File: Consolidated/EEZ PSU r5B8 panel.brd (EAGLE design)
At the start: 316 x 150 mm, 799 parts, among them IC1 LTC3864, IC10 REF5025, IC11 DAC8552, IC12 ADG465SOT-23, IC13 TS5A9411DCKT, IC14 ADS1120, IC15 LP339D, IC16 LM25575, IC17 MC7812, IC18 TPD4E002DRLR, IC19 TPD2E001DZDR, IC2 MC79L05, IC20 ADUM3160BRWZ, IC21 TLC5925IDBQR, IC22 Si8641EC-B-IS1, IC23 SI8651EC-B-IS1, IC24 SI8651EC-B-IS1, IC25 LD1117ADT33TR, IC26 Si8641EC-B-IS1, IC27 PCA21125, IC28 AT25256B, IC29 W5500, IC3 MC78L05, IC30 BC857BS, IC31 TLC555, IC32 SN74LVC2G08DCTR, IC33 TPS3705-33D, IC34 SN74LV1T34DBVR, IC35 SN74LVC2G02DCTR, IC36 DAC8552, IC37 ADS1120, IC38 MCP23S08-E/SO, IC39 OP27GSZ, IC4 LM5574, IC40 TL072D, IC41 TL072D, IC42 REF5025, IC43 LTC3864, IC44 LM5574, IC45 MC79L05, IC46 MC78L05, IC47 TS5A9411DCKT, IC48 ADG465SOT-23, IC49 LP339D, IC5 LP2951SO8, IC50 LP2951SO8, IC6 TL072D, IC7 TL072D, IC8 OP27GSZ, IC9 MCP23S08-E/SO, J1 BS-244DSM-R, J2 BS-244DSM-G, J3 BS-244DSM-B, J4 BS-244DSM-R, J5 BS-244DSM-B, Q1 SUD19P06-60, Q10 MMBT5401, Q11 MMBT5401, Q12 MMBT5551, Q13 MMBT5551, Q14 BSS84P, Q15 2N7002, Q16 MMBT5551, Q17 MMBT5401, Q18 MMBT5551, Q19 MMBT5551, Q2 MMBT5401, Q20 BTA26-600, Q21 BTA26-600, Q22 IRLL014N, Q23 IRLML2246TRPBF, Q24 IRLML2246TRPBF, Q25 IRLML2246TRPBF, Q26 IRLML2246TRPBF, Q27 2N7002, Q28 IRLML2246TRPBF, Q29 2N7002, Q3 2N7002, Q30 2N7002, Q31 IRFP250N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

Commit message: Consolidated PCB, jumpers renumbering
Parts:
- removed JMP1, JMP2: 0R-JUMPA, jump-0r-smd:A0R-JMP
- added JP6, JP7: 0R-JUMPA, jump-0r-smd:A0R-JMP
- C18, C239: value EEEFK1J470P -> EEEFK1J101P
- D28: device diode:DO214AC -> EEZ_Lib1:SOD123
- FB6, FB7: value 2506033007Y3 -> 60R@100MHz
- JP1: value 826926-2 -> 0R-JUMPA; device jumper:JP1 -> jump-0r-smd:A0R-JMP
- JP3: value 0R-JUMPA -> 826926-2; device jump-0r-smd:A0R-JMP -> jumper:JP1
- L16, L2: value See Note 1.2 -> 7443551331
- LED1, LED2: device led:CHIPLED_0805 -> EEZ_Lib1:LED_0805
- R12, R217: value See Note 1.3 -> 324K
- moved JP2 301.9 mm to (15.5, 134.0), turned to 90 degrees
- moved JP1 128.8 mm to (107.6, 125.8), turned to 180 degrees
- moved JP3 80.8 mm to (224.2, 71.1), turned to 90 degrees
- moved JP4 24.5 mm to (307.8, 58.8)
- moved JP5 12.2 mm to (299.5, 42.0)
- renumbered JMP3 to JP8, JMP4 to JP9
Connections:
- net !INT: now also JP2.2; no longer JMP2.2
- net !PS_DRDY: now also JP2.3; no longer JMP2.3
- net !PWD_RST: now also JP3.1; no longer JP1.1
- net +3V3: now also JP4.3; no longer JP2.3
- net +5V: now also JP4.1; no longer JP2.1
- net GND: now also JP3.2; no longer JP1.2
- net INT_EXP: now also JP2.1; no longer JMP2.1
- net MISO: now also JP7.1; no longer JP5.1
- net MODE: now also JP1.2; no longer JMP1.2
- net MOSI: now also JP6.1; no longer JP4.1
- net N$102: now also JP4.2; no longer JP2.2
- net N$104: now also JP7.2; no longer JP5.2
- net N$105: now also JP5.2; no longer JP3.2
- net N$106: now also JP6.2; no longer JP4.2
- net SCLK: now also JP5.1; no longer JP3.1
- net SGND: now also JP1.1; no longer JMP1.1
- net SYNC: now also JP1.3; no longer JMP1.3
- net TOUCH_DIN: now also JP6.3; no longer JP4.3
- net TOUCH_DOUT: now also JP7.3; no longer JP5.3
- net TOUCH_SCLK: now also JP5.3; no longer JP3.3
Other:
- board text added: "JP6"
- board text added: "JP7"
- board text removed: "Alu thermal bridge (5mm thick)"
- board text removed: "Copy here Power module for final panel!"
- board text removed: "JMP1"
- board text removed: "JMP2"

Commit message: Fixed fan control, miniMELF replaced with SOD-323
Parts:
- added C240: EEEFK1J101P, EEZ_Lib1:PANASONIC_F
- added D47: SKL16, EEZ_Lib1:SOD123
- C104: value 470n/100V -> 100n; device rcl:C1812 -> rcl:C0603
- C105, C110: value 10n -> 470n/100V; device rcl:C1206 -> rcl:C1812
- C106, C111: value UPW1J150MED -> 10n; device MyLib6:CAPAE660X610N_COMBO2 -> rcl:C1206
- C107: value 10u -> UPW1J150MED; device rcl:C1206 -> MyLib6:CAPAE660X610N_COMBO2
- C108: value 10n -> 10u
- C109: value 470n/100V -> 10n; device rcl:C1812 -> rcl:C1206
- C112: value 10n -> UPW1J150MED; device rcl:C1206 -> MyLib6:CAPAE660X610N_COMBO2
- C113: value 100n -> 10n; device rcl:C0603 -> rcl:C1206
- C119: value 47u -> 100n; device MyLib6:PANASONIC_C -> rcl:C0603
- C120: value 10u -> 47u
- C121: value 100n -> 10u; device rcl:C0603 -> MyLib6:PANASONIC_C
- C125: value 10u -> 100n; device rcl:C1206 -> rcl:C0603
- C126, C162: value 100n -> 10u; device rcl:C0603 -> rcl:C1206
- C127: value EECS5R5H105 -> 100n; device EEZ_Lib1:SG-R20MM -> rcl:C0603
- C128: value 100n -> EECS5R5H105; device rcl:C0603 -> EEZ_Lib1:SG-R20MM
- C130: value 22n -> 100n; device rcl:C0805 -> rcl:C0603
- C131: value 18p -> 22n
- C132: value 6n8 -> 18p; device rcl:C0603 -> rcl:C0805
- C133: value 10n -> 6n8; device rcl:C0805 -> rcl:C0603
- C134: value 6n8 -> 10n; device rcl:C0603 -> rcl:C0805
- C135: value 18p -> 6n8; device rcl:C0805 -> rcl:C0603
- C136: value 100n -> 18p; device rcl:C0603 -> rcl:C0805
- C144: value 10u -> 100n; device EEZ_Lib1:EC1206 -> rcl:C0603
- C145, C193, C223: value 4u7 -> 10u
- C146: value 10n -> 4u7; device rcl:C0805 -> EEZ_Lib1:EC1206
- C147, C156, C178, C183: value 100n -> 10n; device rcl:C0603 -> rcl:C0805
- C148, C152: value 47n -> 100n; device rcl:C0805 -> rcl:C0603
- C149, C153, C99: value 100n -> 47n; device rcl:C0603 -> rcl:C0805
- C154: value 10n -> 100n; device rcl:C0805 -> rcl:C0603
- C158, C174: value 1n -> 100n; device rcl:C0805 -> rcl:C0603
- C159: value 100n -> 1n; device rcl:C0603 -> rcl:C0805
- C160: value 120p -> 100n; device rcl:C0805 -> rcl:C0603
- C161: value 10u -> 120p; device rcl:C1206 -> rcl:C0805
- C168: value 47p -> 100n; device rcl:C0805 -> rcl:C0603
- C169, C171: value 2n2 -> 47p
- C170: value 47p -> 2n2
- C172: value 100n -> 2n2; device rcl:C0603 -> rcl:C0805
- C177: value 10n -> 1n
- C179, C185: value 1u -> 100n; device rcl:C0805 -> rcl:C0603
- C180, C182: value 10n -> 1u
- C181: value 1u -> 10n
- C188: value 470n -> 1u; device rcl:C1812 -> rcl:C0805
- C189: value 4u7 -> 470n; device rcl:C1210 -> rcl:C1812
- C190: value 10u -> 4u7
- C191: value 330p -> 10u; device rcl:C0805 -> rcl:C1210
- C192: value 10u -> 330p; device rcl:C1210 -> rcl:C0805
- C194: value 4n7 -> 4u7; device rcl:C0805 -> rcl:C1210
- C195: value 120p -> 4n7
- C196: value 1u -> 120p; device rcl:C1206 -> rcl:C0805
- C197: value 470n -> 1u; device rcl:C0805 -> rcl:C1206
- C198: value 100n -> 470n
- C201: value 1u -> 100n; device resistor:C1206 -> rcl:C0805
- C203: value 2u2 -> 1u; device rcl:C0805 -> resistor:C1206
- C204: value 47u -> 2u2; device EEZ_Lib1:CAPAE660X610N -> rcl:C0805
- C206: value 2u2 -> 47u; device rcl:C0805 -> EEZ_Lib1:CAPAE660X610N
- C207: value 330n -> 2u2
- C208: value 3n3 -> 330n
- C209: value 1n -> 3n3
- C210: value 22n -> 1n
- C211: value 100n -> 22n
- C212: value 10n -> 100n
- C213: value 2u2/100V -> 10n; device rcl:C1210 -> rcl:C0805
- C214: value 2u2 -> 2u2/100V; device rcl:C0805 -> rcl:C1210
- C216: value 330p -> 2u2
- C217: value 2m2 -> 330p; device EEZ_Lib1:ECAP7.5/18 -> rcl:C0805
- C218: value 330n -> 2m2; device rcl:C0805 -> EEZ_Lib1:ECAP7.5/18
- C219: value 100n -> 330n
- C222: value 10u -> 100n; device EEZ_Lib1:EC1206 -> rcl:C0805
- C224: value 2m2 -> 4u7; device EEZ_Lib1:ECAP7.5/18 -> EEZ_Lib1:EC1206
- C225: value EEEFK1J470P -> 2m2; device Panasonic-EEEFK_EEEFP:CAPAE830X1050N -> EEZ_Lib1:ECAP7.5/18
- C226: value 470p -> EEEFK1J470P; device rcl:C0805 -> Panasonic-EEEFK_EEEFP:CAPAE830X1050N
- C227: value 4u7 -> 470p; device rcl:C1210 -> rcl:C0805
- C228: value 10n -> 4u7; device rcl:C0805 -> rcl:C1210
- C230: value 2n2 -> 10n
- C231: value 100n -> 2n2; device rcl:C1206 -> rcl:C0805
- C234: device rcl:C0603 -> rcl:C1206
- C235: value 3n3 -> 100n; device rcl:C0805 -> rcl:C0603
- C239: value EEEFK1J101P -> 3n3; device EEZ_Lib1:PANASONIC_F -> rcl:C0805
- C97: value 100u -> 10u; device EEZ_Lib1:CAPAE660X610N -> MyLib6:PANASONIC_C
- C98: value 47n -> 100u; device rcl:C0805 -> EEZ_Lib1:CAPAE660X610N
- D25: value SMBJ5.0A-TR -> BAS316; device MyLib6:DO214AA -> diode:SOD323-W
- D26: value BAS316 -> SMBJ5.0A-TR; device diode:SOD323-W -> MyLib6:DO214AA
- D27: value BAT54S -> BAS316; device diode:SOT23 -> diode:SOD323-W
- D28: value SKL16 -> BAT54S; device EEZ_Lib1:SOD123 -> diode:SOT23
- D29: value BAS316 -> SKL16; device diode:SOD323-W -> EEZ_Lib1:SOD123
- D37: value STPS15H100 -> BAS316; device EEZ_Lib1:TO252 -> diode:SOD323-W
- D38: value BAS316 -> STPS15H100; device diode:SOD323-W -> EEZ_Lib1:TO252
- D39: value DFLS1100-7 -> BAS316; device EEZ_Lib1:SOD123 -> diode:SOD323-W
- D41: value STPS15H100 -> DFLS1100-7; device EEZ_Lib1:TO252@1 -> EEZ_Lib1:SOD123
- D45: value SKL16 -> STPS15H100; device EEZ_Lib1:SOD123 -> EEZ_Lib1:TO252@1
- ZD13, ZD4: value 13V -> BZX384-C15.115; device EEZ_Lib1:MINIMELF -> EEZ_Lib1:SOD323-W
- ZD14, ZD5: value 6V2 -> PDZ6.2B; device EEZ_Lib1:MINIMELF -> EEZ_Lib1:SOD323-W
- moved D25 192.5 mm to (119.5, 52.1), turned to 0 degrees
- moved C119 165.9 mm to (135.4, 61.0), turned to 90 degrees
- moved EEZ_SIGNATURE 128.8 mm to (3.81, 79.8)
- moved EEZ_SIGNATURE3 128.8 mm to (155.8, 79.8)
- moved C104 125.8 mm to (68.7, 64.7)
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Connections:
- removed net GND7: C157.1, C159.1, C161.2, C162.1, C163.1, C164.2, C165.1, C166.1, C167.1, C172.1, C173.2, C177.2, C178.2, C179.1, C180.1, C181.1, C182.1, C183.1, C184.1, C185.1, C186.1, C187.2, C188.2, C189.2, C190.2, C192.2, C193.2, C196.2, C203.2, C204.1, C205.2, C206.2, C207.1, C208.1, C211.1, C212.2, C213.2, C214.2, C215.2, C217.-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
- removed net N$169 (its old number): C160.1, D30.C, IC40.2, R165.2, R178.2
- removed net N$176 (its old number): C171.1, R202.2, R204.1
- removed net N$198 (its old number): D36.A, Q39.C, Q42.1, R186.2
- removed net N$211 (its old number): C158.1, R175.1
- removed net N$214 (its old number): C187.1, IC42.5
- removed net N$220 (its old number): C160.2, R216.1
- removed net N$229 (its old number): C198.2, IC43.4
- removed net N$234 (its old number): C209.2, R230.2
- removed net N$239 (its old number): C211.2, IC44.1
- removed net N$243 (its old number): C216.2, R235.2
- removed net N$251 (its old number): C228.2, Q47.B, R244.1, R245.2, R246.2
- removed net N$254 (its old number): C229.1, Q46.B, R247.2, R248.1
- removed net N$257 (its old number): C223.+, FB12.P$1, IC50.1, R237.1, R239.1
- removed net N$259 (its old number): C235.2, IC37.10, R255.2
- new net GND1: C158.1, C160.1, C162.2, C163.1, C164.1, C165.2, C166.1, C167.1, C168.1, C173.1, C174.2, C178.2, C179.2, C180.1, C181.1, C182.1, C183.1, C184.1, C185.1, C186.1, C187.1, C188.2, C189.2, C190.2, C191.2, C193.2, C194.2, C197.2, C204.2, C205.1, C206.2, C207.2, C208.1, C209.1, C212.1, C213.2, C214.2, C215.2, C216.2, C218.-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
- new net N$163: D21.C, X6.3
- new net N$173: C166.2, C186.2, IC37.12, R166.2
- new net N$197: D36.C, ZD14.C
- new net N$199: D37.A, Q39.C, Q42.1, R186.2
- new net N$212: C159.1, R175.1
- new net N$215: C188.1, IC42.5
- new net N$227: C198.1, IC43.9
- new net N$233: C204.1, D41.A, L13.1
- new net N$237: C211.2, IC44.16
- new net N$242: C213.1, IC44.10
- new net N$246: C221.1, D47.C, FB11.P$1, IC46.1
- new net N$253: C231.2, Q47.C, R249.1, R251.2
- new net N$256: C231.1, Q48.B, R249.2, R250.2
- new net N$258: C224.+, FB12.P$1, IC50.1, R237.1, R239.1
- new net N$263: C239.1, IC37.6, R258.2
- net !MR: now also C153.2; no longer C152.2
- net +3V3: now also C108.1, C116.1, C118.1, C121.1, C123.1, C127.1, C131.1, C137.2, C144.1, C145.+, C150.2, C151.1, C152.2, C154.1, C157.1, D27.A; no longer C107.1, C114.1, C117.1, C120.1, C122.1, C126.1, C130.1, C136.2, C138.1, C144.+, C149.2, C150.1, C151.2, C153.1, C156.1, D26.A
- net +5V: now also C100.1, C120.1, C126.2, D26.C; no longer C119.1, C125.2, C99.1, D25.C
- net +5V1: now also C163.2, C165.1, C167.2, C187.2; no longer C162.2, C164.1, C166.2, C186.2
- net +VNR1: now also C207.1, C220.1; no longer C206.1, C218.1
- net +VREF1: now also C164.2, C223.+, C235.2; no longer C163.2, C222.+, C234.2
- net -9V1: now also C205.2, C208.2; no longer C204.2, C207.2
- net 12VDC: now also C98.1
- net 1V2O: now also C147.2; no longer C146.2
- net AC_IN1: now also X2.1; no longer X2.2
- net AC_IN2: now also X2.2; no longer X2.1
- net AC_IN3: now also D42.1, D42.2, D44.3, X22.2; no longer D41.1, D41.2, D43.3, X22.1
- net AC_IN4: now also D43.1, D43.2, D45.3, X22.1; no longer D42.1, D42.2, D44.3, X22.2
- net AUX_FAN_SENSE: now also D21.A; no longer X6.3
- net CH1_GND: now also C114.2, C117.2, C148.2, C149.1; no longer C113.2, C116.2, C147.2, C148.1
- net CH1_VDD: now also C114.1, C117.1, C148.1; no longer C113.1, C116.1, C147.1
- net CH2_GND: now also C119.2, C122.2; no longer C118.2, C121.2
- net CH2_VDD: now also C119.1, C122.1; no longer C118.1, C121.1
- net DC+: now also L1.2; no longer L1.1
- net DC+1: now also C234.2, L17.2; no longer C233.2, L17.1
- net DC-: now also L1.1, X1.3; no longer L1.2, X1.1
- net DC-1: now also C234.1, L17.1, X23.3; no longer C233.1, L17.2, X23.1
- net DC_OUT: now also L1.3; no longer L1.4
- net DC_OUT1: now also C190.1, C194.1, C197.1, C198.2, C218.+, C225.+, C228.1, C232.2, D43.3, L17.3; no longer C188.1, C193.1, C196.1, C197.2, C217.+, C224.+, C227.1, C231.2, D41.3, L17.4
- net DC_PREG3: now also C214.1; no longer C213.1
- net EARTH: now also C106.2, C109.1, C111.2, C113.1, C131.2, C134.2, X1.1; no longer C105.2, C108.1, C110.2, C112.1, C130.2, C133.2, X1.3
- net EARTH1: now also C232.1, C233.2, X23.1; no longer C231.1, C232.2, X23.3
- net ENC_A: now also C155.2, MCU.A8; no longer C154.2, MCU.A14
- net ENC_B: now also C156.1, MCU.A9; no longer C155.1, MCU.A15
- net ETH_IN+: now also C135.1; no longer C134.1
- net ETH_IN-: now also C133.1; no longer C132.1
- net FAN_OUT: now also C99.2; no longer C98.2
- net GND: now also C100.2, C103.2, C108.2, C116.2, C118.2, C121.2, C123.2, C126.1, C128.2, C130.1, C132.2, C136.2, C138.1, C144.2, C145.-, C147.1, C150.1, C151.2, C153.1, C154.2, C155.1, C157.2, C97.2, D26.A, D28.1, IC16.TP, L1.4; no longer C102.2, C107.2, C114.2, C117.2, C119.2, C122.2, C123.1, C126.2, C128.1, C131.2, C135.2, C136.1, C138.2, C144.-, C146.1, C149.1, C150.2, C151.1, C153.2, C154.1, C155.2, C99.2, D21.A, D27.1, L1.3
- net GNDA: now also C146.-; no longer C145.-
- net IS2: now also D40.A; no longer D39.A
- net I_SERVO1: now also C159.2, D30.A, D33.C; no longer C158.2, D29.A, D32.C
- net L_OUT12: now also C191.1, C193.1, C240.1; no longer C190.1, C192.1, C239.1
- net N$107: now also C128.1; no longer C127.1
- net N$109: now also C124.2, D27.C; no longer C123.2, D26.C
- net N$111: now also C132.1; no longer C131.1
- net N$112: now also C136.1; no longer C135.1
- net N$113: now also C133.2; no longer C132.2
- net N$115: now also C135.2; no longer C134.2
- net N$124: now also C134.1; no longer C133.1
- net N$132: now also C138.2; no longer C137.2
- net N$136: now also C149.2; no longer C148.2
- net N$139: now also D28.3; no longer D27.3
- net N$144: now also D28.2; no longer D27.2
- net N$148: now also D29.C; no longer D28.C
- net N$149: now also D29.A; no longer D28.A
- net N$155: now also D23.C; no longer D22.C
- net N$156: now also D24.C; no longer D23.C
- net N$171: now also C161.1, D31.C, IC40.2, R165.2, R178.2; no longer C165.2, C185.2, IC37.12, R166.2
- net N$178: now also C172.1, R202.2, R204.1; no longer C169.1, R201.2, R203.1
- net N$181: now also C170.1, R201.2, R203.1; no longer C168.2, R173.1
- net N$182: now also C169.2, R173.1; no longer C170.2, R174.1
- net N$185: now also C171.2, R174.1; no longer C174.2, R176.1
- net N$187: now also C175.2, R176.1; no longer D29.C, IC41.2, R160.2, R175.2, R176.2
- net N$188: now also D30.C, IC41.2, R160.2, R175.2, R176.2; no longer C175.2, R177.1
- net N$189: now also R177.1; no longer R178.1
- net N$190: now also C177.2, R178.1; no longer D31.A, D32.A, R179.1
- net N$191: now also D32.A, D33.A, R179.1; no longer D33.C, D35.A, Q31.G, R181.1
- net N$192: now also D34.C, D36.A, Q31.G, R181.1; no longer D33.A, Q32.3
- net N$193: now also Q32.3; no longer Q32.1, R180.1, R182.2
- net N$194: now also D35.A, Q32.1, R180.1, R182.2; no longer D34.C, Q34.C, ZD13.C
- net N$195: now also D35.C, Q34.C, ZD13.C; no longer C177.1, R182.1
- net N$196: now also C178.1, R182.1; no longer D35.C, ZD14.C
- net N$221: now also C161.2, R216.1; no longer C191.2, R219.2
- net N$222: now also C192.2, R219.2; no longer C226.2, D38.A, Q43.B, R220.1, R222.2
- net N$223: now also C227.2, D39.A, Q43.B, R220.1, R222.2; no longer D38.C, Q43.E, R221.2
- net N$224: now also D39.C, Q43.E, R221.2; no longer C195.1, IC43.6, R225.2
- net N$225: now also C196.1, IC43.6, R225.2; no longer C194.1, R225.1
- net N$226: now also C195.1, R225.1; no longer C197.1, IC43.9
- net N$230: now also C199.2, IC43.4; no longer C226.1, Q43.C, Q45.3, R241.1
- net N$231: now also C227.1, Q43.C, Q45.3, R241.1; no longer C199.2, C201.1, L11.1, L12.2, R226.1, R243.2
- net N$232: now also C200.2, C202.1, L11.1, L12.2, R226.1, R243.2; no longer C203.1, D40.A, L13.1
- net N$235: now also C210.2, R230.2; no longer C209.1, IC44.6, R231.2, R232.1
- net N$236: now also C210.1, IC44.6, R231.2, R232.1; no longer C210.2, IC44.16
- net N$240: now also C212.2, IC44.1; no longer C208.2, IC44.8
- net N$241: now also C209.2, IC44.8; no longer C212.1, IC44.10
- net N$244: now also C217.2, R235.2; no longer C221.2, D45.A, FB9.P$1, IC45.1
- net N$245: now also C222.2, D46.A, FB9.P$1, IC45.1; no longer C220.1, D46.C, FB11.P$1, IC46.1
- net N$252: now also C229.2, Q47.B, R244.1, R245.2, R246.2; no longer C230.2, Q47.C, R249.1, R251.2
- net N$255: now also Q46.B, R247.2, R248.1; no longer Q48.B, R249.2, R250.2
- net N$260: now also IC37.10, R255.2; no longer IC37.7, R256.2
- net N$261: now also IC37.7, R256.2; no longer IC37.11, R257.2
- net N$262: now also C238.2, IC37.11, R257.2; no longer C238.1, IC37.6, R258.2
- net N$84: now also C99.1; no longer C98.1
- net N$86: now also C98.2; no longer C97.2
- net N$87: now also C104.1; no longer C103.1
- net N$90: now also C101.1; no longer C100.1
- net N$91: now also C103.1; no longer C102.1
- net N$92: now also D22.C; no longer D21.C
- net N$93: now also D25.C; no longer D24.C
- net N$94: now also C105.2; no longer C104.2
- net N$95: now also C110.2; no longer C109.2
- net NTC1: now also C125.2; no longer C124.2
- net NTC2: now also C130.2; no longer C129.2
- net OUT+1: now also C170.2, C175.1, C177.1, C229.1; no longer C169.2, C174.1, C176.1, C228.1
- net OUT-1: now also C172.2, C176.1, C230.2; no longer C171.2, C175.1, C229.2
- net OUT1+: now also C106.1; no longer C105.1
- net OUT1-: now also C107.2, C107.2.1, C109.2; no longer C106.2, C106.2.1, C108.2
- net OUT2+: now also C112.1, C112.1.1; no longer C109.1, C111.1.1
- net OUT2-: now also C113.2; no longer C112.2
- net POUT-1: now also C200.1, C203.2, C226.2; no longer C199.1, C200.2, C225.2
- net PWR_IN1+: now also C105.1, C107.1, C107.1.1; no longer C104.1, C106.1, C106.1.1
- net PWR_IN2-: now also C112.2, C112.2.1; no longer C111.2, C111.2.1
- net P_OUT1: now also C201.1, C203.1, C226.1; no longer C200.1, C202.1, C225.1
- net Q9C1: now also D37.C; no longer D36.C
- net SENSE+1: now also C169.1; no longer C168.1
- net SENSE-1: now also C171.1; no longer C170.1
- net SGND1: now also C196.2, C199.1; no longer C194.2, C198.1
- net SW3: now also C192.1, D38.3; no longer C191.1, D37.3
- net SW4: now also C211.1, C217.1, D40.C; no longer C210.1, C216.1, D39.C
- net TEMP_ANALOG: now also C129.2; no longer C128.2
- net TOCAP: now also C146.+; no longer C145.+
- net U_SERVO1: now also D31.A, D32.C; no longer D30.A, D31.C
- net V+1: now also C158.2, C162.1, C168.2, C174.1, C180.2, C184.2; no longer C157.2, C161.1, C167.2, C173.1, C179.2, C182.2
- net V-1: now also C160.2, C173.2, C179.1, C182.2, C185.2; no longer C159.2, C172.2, C178.1, C180.2, C184.2
- net VOUT+1: now also C206.1, C216.1; no longer C205.1, C214.1
- net VOUT-1: now also D41.C; no longer D40.C
- net XUSB_GND: now also C101.2, C102.1, C104.2; no longer C100.2, C101.1, C103.2
- net XUSB_VBUS: now also C102.2; no longer C101.2
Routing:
- net GND7: track 244.4 -> 0.00 mm, vias 135 -> 0
- net GND1: track 0.00 -> 241.5 mm, vias 0 -> 135
- net N$190: track 53.2 -> 3.14 mm, vias 2 -> 0
- net N$253: track 0.00 -> 45.4 mm, vias 0 -> 2
- net N$252: track 45.4 -> 8.81 mm, vias 2 -> 0
- net N$163: track 0.00 -> 30.0 mm
- net N$191: track 24.4 -> 53.2 mm, vias 1 -> 2
- net N$169 (its old number): track 21.8 -> 0.00 mm
- net N$192: track 3.63 -> 24.4 mm, vias 0 -> 1
- net N$195: track 2.04 -> 21.6 mm
- net EARTH1: track 52.0 -> 33.8 mm, vias 1 -> 0
- net EARTH: track 239.5 -> 221.4 mm, vias 2 -> 1
- net N$258: track 0.00 -> 17.9 mm
- net N$257 (its old number): track 17.9 -> 0.00 mm
- net N$199: track 0.00 -> 17.4 mm
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- added copper zone on layer 1, net GND1
- added copper zone on layer 16, net GND1
- removed copper zone on layer 1, net GND7
- removed copper zone on layer 16, net GND7
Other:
- board text added: "C157"
- board text added: "D29"
- board text added: "DC in max. 62V"
- board text removed: "DC in"
- board text removed: "max. 62V"

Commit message: Missed hole added to Power board, minor bottom silk mask changes
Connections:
- new net +5V2: C120.1, C126.2, D26.C, FB8.P$1, IC25.3, JP4.1, LED_CC1.A, LED_CC2.A, LED_CV1.A, LED_CV2.A, LED_O1.A, LED_O2.A, LED_PROG1.A, LED_PROG2.A, LED_PWR.A, LED_S1.A, LED_S2.A, LED_SP.A, MCU.5V, Q23.2, Q24.2, Q25.2, Q26.2, R122.2, R123.2, R125.2, R127.2, SG1.+, SG1.+B, SW1.3, X20.2
- new net EARTH2: C106.2, C109.1, C111.2, C113.1, C131.2, C134.2, J2.P$1, X12.3, X12.3.1, X14.1, X14.1.1, X18.3
- new net GND7: C108.2, C115.2, C116.2, C118.2, C120.2, C121.2, C123.2, C124.1, C125.1, C126.1, C127.2, C128.2, C129.1, C130.1, C132.2, C136.2, C137.1, C138.1, C139.2, C140.2, C141.2, C142.2, C143.2, C144.2, C145.-, C147.1, C150.1, C151.2, C152.1, C153.1, C154.2, C155.1, C156.2, C157.2, D22.A, D23.A, D24.A, D25.A, D26.A, D28.1, IC21.1, IC22.2, IC22.8, IC23.8, IC24.8, IC25.1, IC26.2, IC26.8, IC27.7, IC28.4, IC29.29, IC32.4, IC33.3, IC33.4, IC34.3, IC35.4, JP3.2, K_PAR.A1, K_S1.8, K_S2.8, K_SER.A1, LCD1.1, MCU.GND, MCU.GND1, MCU.GND2, MCU.GND3, MCU.GND4, MCU.ICSP_GND, OK3.3, Q27.2, Q29.2, Q30.2, R126.1, R129.2, R131.1, R132.2, R133.2, R145.1, R149.2, R150.2, RN1.5, RN1.6, RN1.7, RN1.8, RN2.5, SH3.P$1, SW2.1, SW2.2, SW2.5, WIFI.1, X12.1, X12.1.1, X16.1, X16.2, X16.9, X19.4, X20.4, ZD12.A
- net +5V: no longer C120.1, C126.2, D26.C, FB8.P$1, IC25.3, JP4.1, LED_CC1.A, LED_CC2.A, LED_CV1.A, LED_CV2.A, LED_O1.A, LED_O2.A, LED_PROG1.A, LED_PROG2.A, LED_PWR.A, LED_S1.A, LED_S2.A, LED_SP.A, MCU.5V, Q23.2, Q24.2, Q25.2, Q26.2, R122.2, R123.2, R125.2, R127.2, SG1.+, SG1.+B, SW1.3, X20.2
- net EARTH: no longer C106.2, C109.1, C111.2, C113.1, C131.2, C134.2, J2.P$1, X12.3, X12.3.1, X14.1, X14.1.1, X18.3
- net GND: no longer C108.2, C115.2, C116.2, C118.2, C120.2, C121.2, C123.2, C124.1, C125.1, C126.1, C127.2, C128.2, C129.1, C130.1, C132.2, C136.2, C137.1, C138.1, C139.2, C140.2, C141.2, C142.2, C143.2, C144.2, C145.-, C147.1, C150.1, C151.2, C152.1, C153.1, C154.2, C155.1, C156.2, C157.2, D22.A, D23.A, D24.A, D25.A, D26.A, D28.1, IC21.1, IC22.2, IC22.8, IC23.8, IC24.8, IC25.1, IC26.2, IC26.8, IC27.7, IC28.4, IC29.29, IC32.4, IC33.3, IC33.4, IC34.3, IC35.4, JP3.2, K_PAR.A1, K_S1.8, K_S2.8, K_SER.A1, LCD1.1, MCU.GND, MCU.GND1, MCU.GND2, MCU.GND3, MCU.GND4, MCU.ICSP_GND, OK3.3, Q27.2, Q29.2, Q30.2, R126.1, R129.2, R131.1, R132.2, R133.2, R145.1, R149.2, R150.2, RN1.5, RN1.6, RN1.7, RN1.8, RN2.5, SH3.P$1, SW2.1, SW2.2, SW2.5, WIFI.1, X12.1, X12.1.1, X16.1, X16.2, X16.9, X19.4, X20.4, ZD12.A
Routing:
- net +5V2: track 0.00 -> 593.2 mm, vias 0 -> 18
- net +5V: track 902.9 -> 309.7 mm, vias 29 -> 11
- net EARTH2: track 0.00 -> 187.5 mm, vias 0 -> 1
- net GND: track 500.0 -> 328.8 mm, vias 280 -> 168
- net GND7: track 0.00 -> 171.2 mm, vias 0 -> 112
- net EARTH: track 221.4 -> 55.8 mm
- net EARTH1: track 33.8 -> 55.8 mm, vias 0 -> 1
- added copper zone on layer 1, net GND7
- added copper zone on layer 16, net GND7

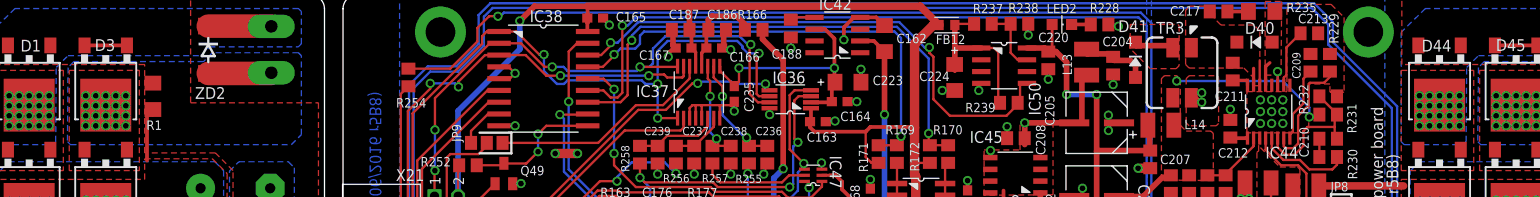
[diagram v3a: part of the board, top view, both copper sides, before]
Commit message: Consolidated BOM for PCBA, AUX PS BOM update, Power module PCB update
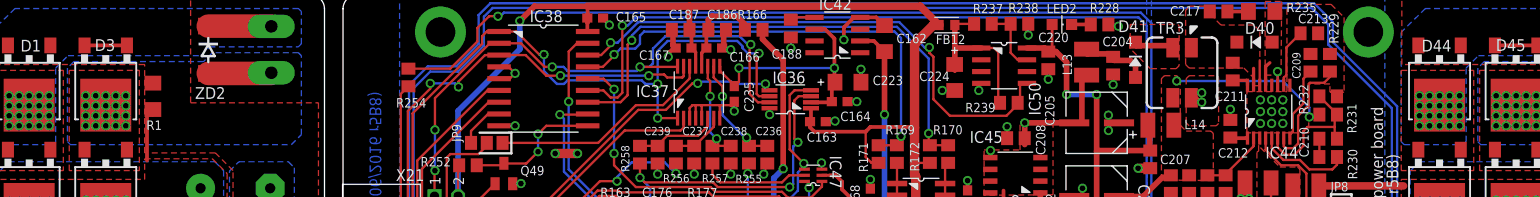
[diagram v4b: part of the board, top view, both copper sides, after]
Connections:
- new net +5V3: C163.2, C165.1, C167.2, C187.2, FB12.P$2, IC36.1, IC37.13, IC38.18, Q33.B, Q41.2, R171.2, R172.2, R198.1, R252.2, X21.2
- new net GND8: C158.1, C160.1, C162.2, C163.1, C164.1, C165.2, C166.1, C167.1, C168.1, C173.1, C174.2, C178.2, C179.2, C180.1, C181.1, C182.1, C183.1, C184.1, C185.1, C186.1, C187.1, C188.2, C189.2, C190.2, C191.2, C193.2, C194.2, C197.2, C204.2, C205.1, C206.2, C207.2, C208.1, C209.1, C212.1, C213.2, C214.2, C215.2, C216.2, C218.-, C219.2, C220.2, C221.2, C222.1, C223.-, C224.-, C225.-, C228.2, C233.1, C235.1, C236.1, C237.1, C238.1, C239.2, C240.2, D38.1, D38.2, D44.1, D44.2, D45.1, D45.2, D46.C, D47.A, GND1.P$1, IC36.8, IC37.3, IC37.4, IC37.5, IC37.8, IC38.4, IC38.5, IC38.9, IC41.5, IC42.4, IC43.TP, IC44.12, IC44.9, IC45.5, IC46.2, IC46.3, IC46.6, IC46.7, IC47.3, IC50.4, L17.4, Q40.2, Q42.2, Q48.E, Q49.E, R168.1, R184.1, R192.1, R197.1, R200.1, R214.1, R215.2, R219.1, R227.2, R228.2, R229.2, R232.2, R234.1, R238.2, R250.1, R253.1, SH4.P$2, SH5.P$2, TP6.GND, TR3.4, X21.10, X21.12, X21.14
- net +5V: no longer C64.1, C68.2, C72.2, C73.2, FB4.P$2, IC11.1, IC14.13, IC9.18, Q13.B, Q14.2, R73.1, R86.2, R92.2, R98.2, X3.2
- net +5V1: now also C64.1, C68.2, C72.2, C73.2, FB4.P$2, IC11.1, IC14.13, IC9.18, Q13.B, Q14.2, R73.1, R86.2, R92.2, R98.2, X3.2; no longer C163.2, C165.1, C167.2, C187.2, FB12.P$2, IC36.1, IC37.13, IC38.18, Q33.B, Q41.2, R171.2, R172.2, R198.1, R252.2, X21.2
- net GND: no longer C10.2, C12.2, C18.2, C20.2, C24.2, C25.1, C26.1, C27.1, C29.2, C3.1, C30.2, C31.2, C33.2, C34.2, C35.2, C36.1, C37.2, C38.2, C39.1, C4.-, C41.2, C42.-, C43.2, C44.2, C5.-, C52.1, C53.2, C54.1, C55.1, C56.1, C57.1, C58.1, C59.2, C6.2, C60.1, C61.1, C64.2, C65.2, C66.-, C67.2, C68.1, C69.1, C7.2, C70.1, C71.2, C72.1, C73.1, C74.1, C75.1, C76.1, C77.1, C78.1, C8.2, C81.1, C82.1, D1.1, D1.2, D3.1, D3.2, D5.1, D5.2, D8.C, D9.A, GND.P$1, IC1.TP, IC10.4, IC11.8, IC13.3, IC14.3, IC14.4, IC14.5, IC14.8, IC2.5, IC3.2, IC3.3, IC3.6, IC3.7, IC4.12, IC4.9, IC5.4, IC7.5, IC9.4, IC9.5, IC9.9, L1.4, Q15.2, Q16.E, Q18.E, Q8.2, R1.2, R17.1, R20.2, R22.2, R25.2, R26.2, R42.1, R44.1, R48.1, R60.1, R75.1, R8.1, R84.1, R91.1, R95.2, R96.1, SH1.P$2, SH2.P$2, TP2.GND, TR1.4, X3.10, X3.12, X3.14
- net GND1: now also C10.2, C12.2, C18.2, C20.2, C24.2, C25.1, C26.1, C27.1, C29.2, C3.1, C30.2, C31.2, C33.2, C34.2, C35.2, C36.1, C37.2, C38.2, C39.1, C4.-, C41.2, C42.-, C43.2, C44.2, C5.-, C52.1, C53.2, C54.1, C55.1, C56.1, C57.1, C58.1, C59.2, C6.2, C60.1, C61.1, C64.2, C65.2, C66.-, C67.2, C68.1, C69.1, C7.2, C70.1, C71.2, C72.1, C73.1, C74.1, C75.1, C76.1, C77.1, C78.1, C8.2, C81.1, C82.1, D1.1, D1.2, D3.1, D3.2, D5.1, D5.2, D8.C, D9.A, GND.P$1, IC1.TP, IC10.4, IC11.8, IC13.3, IC14.3, IC14.4, IC14.5, IC14.8, IC2.5, IC3.2, IC3.3, IC3.6, IC3.7, IC4.12, IC4.9, IC5.4, IC7.5, IC9.4, IC9.5, IC9.9, L1.4, Q15.2, Q16.E, Q18.E, Q8.2, R1.2, R17.1, R20.2, R22.2, R25.2, R26.2, R42.1, R44.1, R48.1, R60.1, R75.1, R8.1, R84.1, R91.1, R95.2, R96.1, SH1.P$2, SH2.P$2, TP2.GND, TR1.4, X3.10, X3.12, X3.14; no longer C158.1, C160.1, C162.2, C163.1, C164.1, C165.2, C166.1, C167.1, C168.1, C173.1, C174.2, C178.2, C179.2, C180.1, C181.1, C182.1, C183.1, C184.1, C185.1, C186.1, C187.1, C188.2, C189.2, C190.2, C191.2, C193.2, C194.2, C197.2, C204.2, C205.1, C206.2, C207.2, C208.1, C209.1, C212.1, C213.2, C214.2, C215.2, C216.2, C218.-, C219.2, C220.2, C221.2, C222.1, C223.-, C224.-, C225.-, C228.2, C233.1, C235.1, C236.1, C237.1, C238.1, C239.2, C240.2, D38.1, D38.2, D44.1, D44.2, D45.1, D45.2, D46.C, D47.A, GND1.P$1, IC36.8, IC37.3, IC37.4, IC37.5, IC37.8, IC38.4, IC38.5, IC38.9, IC41.5, IC42.4, IC43.TP, IC44.12, IC44.9, IC45.5, IC46.2, IC46.3, IC46.6, IC46.7, IC47.3, IC50.4, L17.4, Q40.2, Q42.2, Q48.E, Q49.E, R168.1, R184.1, R192.1, R197.1, R200.1, R214.1, R215.2, R219.1, R227.2, R228.2, R229.2, R232.2, R234.1, R238.2, R250.1, R253.1, SH4.P$2, SH5.P$2, TP6.GND, TR3.4, X21.10, X21.12, X21.14
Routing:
- net GND: track 328.8 -> 87.2 mm, vias 168 -> 33
- net GND8: track 0.00 -> 241.5 mm, vias 0 -> 135
- net +5V3: track 0.00 -> 188.9 mm, vias 0 -> 7
- net +5V: track 309.7 -> 120.8 mm, vias 11 -> 4
- added copper zone on layer 1, net GND8
- added copper zone on layer 16, net GND8

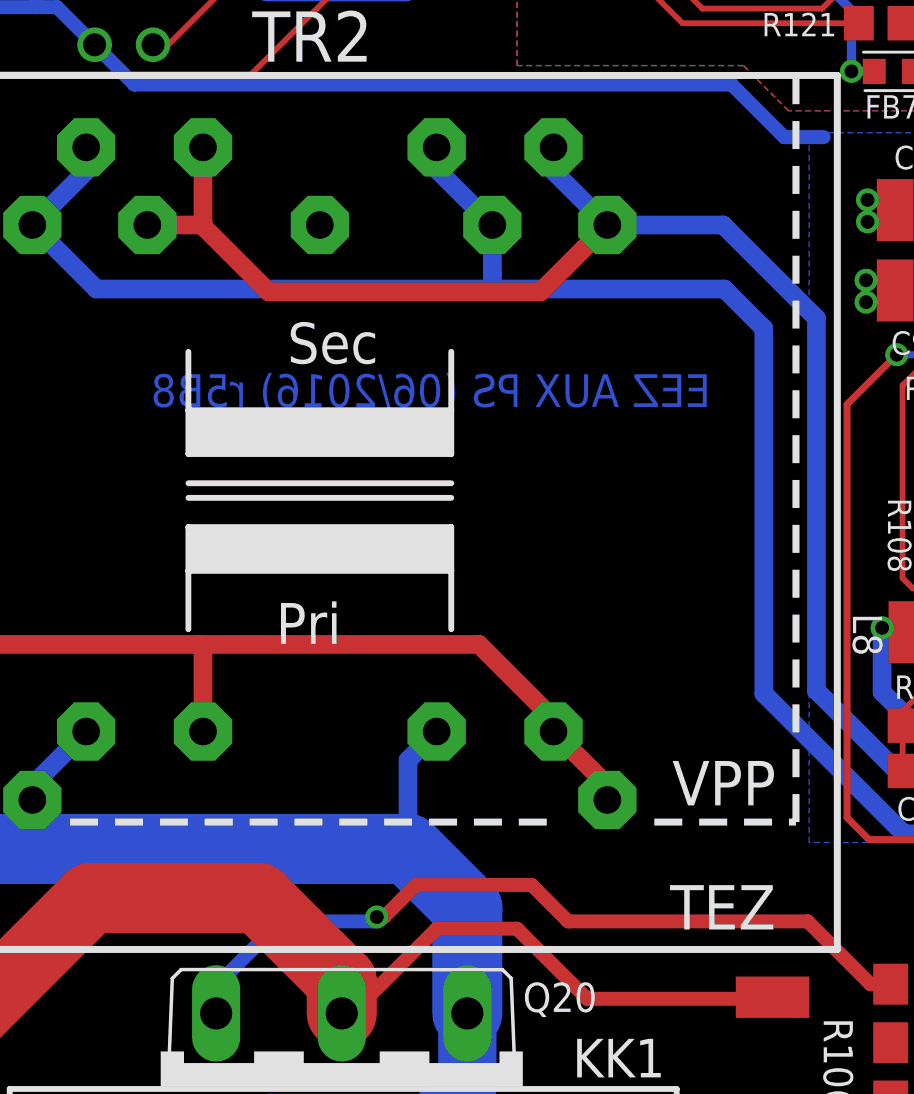
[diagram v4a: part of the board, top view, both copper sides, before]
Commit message: Myrra AC/DC module for 115VAC, BOM updated
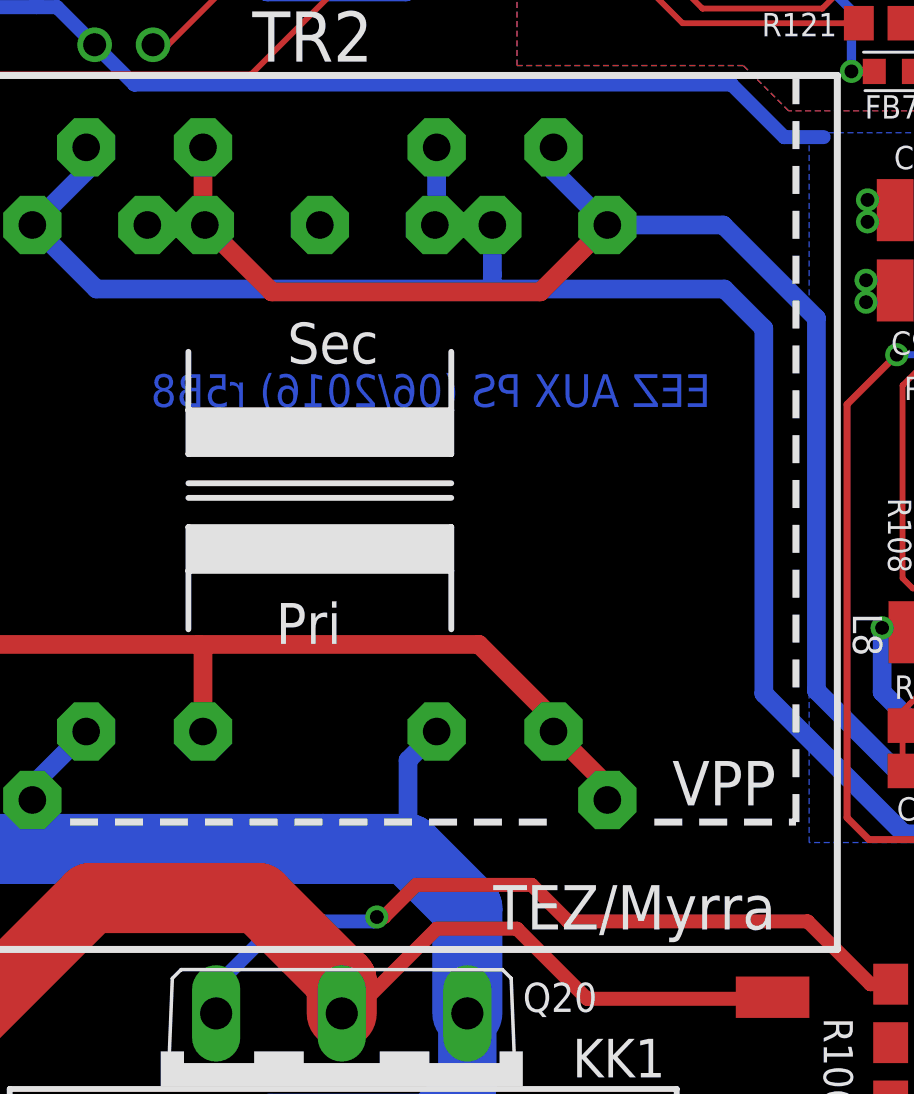
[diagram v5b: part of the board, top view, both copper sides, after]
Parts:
- TR2: device EEZ_Lib1:PCB_TRAFO6VA_TEZ+VPP -> EEZ_Lib1:PCB_TRAFO6VA_7.5W
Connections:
- net N$78: now also TR2.S2M
- net N$80: now also TR2.S1M
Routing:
- net N$80: track 102.2 -> 103.8 mm

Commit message: PCB fiducials, outlines, milling bridges
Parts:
- added U$13, U$14, U$15, U$16, U$19, U$20: FIDUCIAL_2, EEZ_Lib1:FIDUCIAL_DUAL
- added U$17: (no value), olimex_logo1:RECYCLE_BIN1/8
- added U$18: (no value), olimex_logo1:PB_SMALL
- U$11: value (none) -> FIDUCIAL_2; device olimex_logo1:RECYCLE_BIN1/8 -> EEZ_Lib1:FIDUCIAL_DUAL
- U$12: value (none) -> FIDUCIAL_2; device olimex_logo1:PB_SMALL -> EEZ_Lib1:FIDUCIAL_DUAL
- moved U$11 275.6 mm to (3.30, 78.7)
- moved U$12 128.1 mm to (147.6, 120.1)
- moved EEZ_SIGNATURE 66.4 mm to (3.81, 146.3)
- moved EEZ_SIGNATURE3 66.4 mm to (155.8, 146.3)
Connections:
- removed net +5V2: C120.1, C126.2, D26.C, FB8.P$1, IC25.3, JP4.1, LED_CC1.A, LED_CC2.A, LED_CV1.A, LED_CV2.A, LED_O1.A, LED_O2.A, LED_PROG1.A, LED_PROG2.A, LED_PWR.A, LED_S1.A, LED_S2.A, LED_SP.A, MCU.5V, Q23.2, Q24.2, Q25.2, Q26.2, R122.2, R123.2, R125.2, R127.2, SG1.+, SG1.+B, SW1.3, X20.2
- removed net +5V3: C163.2, C165.1, C167.2, C187.2, FB12.P$2, IC36.1, IC37.13, IC38.18, Q33.B, Q41.2, R171.2, R172.2, R198.1, R252.2, X21.2
- removed net EARTH2: C106.2, C109.1, C111.2, C113.1, C131.2, C134.2, J2.P$1, X12.3, X12.3.1, X14.1, X14.1.1, X18.3
- removed net GND7: C108.2, C115.2, C116.2, C118.2, C120.2, C121.2, C123.2, C124.1, C125.1, C126.1, C127.2, C128.2, C129.1, C130.1, C132.2, C136.2, C137.1, C138.1, C139.2, C140.2, C141.2, C142.2, C143.2, C144.2, C145.-, C147.1, C150.1, C151.2, C152.1, C153.1, C154.2, C155.1, C156.2, C157.2, D22.A, D23.A, D24.A, D25.A, D26.A, D28.1, IC21.1, IC22.2, IC22.8, IC23.8, IC24.8, IC25.1, IC26.2, IC26.8, IC27.7, IC28.4, IC29.29, IC32.4, IC33.3, IC33.4, IC34.3, IC35.4, JP3.2, K_PAR.A1, K_S1.8, K_S2.8, K_SER.A1, LCD1.1, MCU.GND, MCU.GND1, MCU.GND2, MCU.GND3, MCU.GND4, MCU.ICSP_GND, OK3.3, Q27.2, Q29.2, Q30.2, R126.1, R129.2, R131.1, R132.2, R133.2, R145.1, R149.2, R150.2, RN1.5, RN1.6, RN1.7, RN1.8, RN2.5, SH3.P$1, SW2.1, SW2.2, SW2.5, WIFI.1, X12.1, X12.1.1, X16.1, X16.2, X16.9, X19.4, X20.4, ZD12.A
- removed net GND8: C158.1, C160.1, C162.2, C163.1, C164.1, C165.2, C166.1, C167.1, C168.1, C173.1, C174.2, C178.2, C179.2, C180.1, C181.1, C182.1, C183.1, C184.1, C185.1, C186.1, C187.1, C188.2, C189.2, C190.2, C191.2, C193.2, C194.2, C197.2, C204.2, C205.1, C206.2, C207.2, C208.1, C209.1, C212.1, C213.2, C214.2, C215.2, C216.2, C218.-, C219.2, C220.2, C221.2, C222.1, C223.-, C224.-, C225.-, C228.2, C233.1, C235.1, C236.1, C237.1, C238.1, C239.2, C240.2, D38.1, D38.2, D44.1, D44.2, D45.1, D45.2, D46.C, D47.A, GND1.P$1, IC36.8, IC37.3, IC37.4, IC37.5, IC37.8, IC38.4, IC38.5, IC38.9, IC41.5, IC42.4, IC43.TP, IC44.12, IC44.9, IC45.5, IC46.2, IC46.3, IC46.6, IC46.7, IC47.3, IC50.4, L17.4, Q40.2, Q42.2, Q48.E, Q49.E, R168.1, R184.1, R192.1, R197.1, R200.1, R214.1, R215.2, R219.1, R227.2, R228.2, R229.2, R232.2, R234.1, R238.2, R250.1, R253.1, SH4.P$2, SH5.P$2, TP6.GND, TR3.4, X21.10, X21.12, X21.14
- net +5V: now also C120.1, C126.2, C64.1, C68.2, C72.2, C73.2, D26.C, FB4.P$2, FB8.P$1, IC11.1, IC14.13, IC25.3, IC9.18, JP4.1, LED_CC1.A, LED_CC2.A, LED_CV1.A, LED_CV2.A, LED_O1.A, LED_O2.A, LED_PROG1.A, LED_PROG2.A, LED_PWR.A, LED_S1.A, LED_S2.A, LED_SP.A, MCU.5V, Q13.B, Q14.2, Q23.2, Q24.2, Q25.2, Q26.2, R122.2, R123.2, R125.2, R127.2, R73.1, R86.2, R92.2, R98.2, SG1.+, SG1.+B, SW1.3, X20.2, X3.2
- net +5V1: now also C163.2, C165.1, C167.2, C187.2, FB12.P$2, IC36.1, IC37.13, IC38.18, Q33.B, Q41.2, R171.2, R172.2, R198.1, R252.2, X21.2; no longer C64.1, C68.2, C72.2, C73.2, FB4.P$2, IC11.1, IC14.13, IC9.18, Q13.B, Q14.2, R73.1, R86.2, R92.2, R98.2, X3.2
- net EARTH: now also C106.2, C109.1, C111.2, C113.1, C131.2, C134.2, J2.P$1, X12.3, X12.3.1, X14.1, X14.1.1, X18.3
- net GND: now also C10.2, C108.2, C115.2, C116.2, C118.2, C12.2, C120.2, C121.2, C123.2, C124.1, C125.1, C126.1, C127.2, C128.2, C129.1, C130.1, C132.2, C136.2, C137.1, C138.1, C139.2, C140.2, C141.2, C142.2, C143.2, C144.2, C145.-, C147.1, C150.1, C151.2, C152.1, C153.1, C154.2, C155.1, C156.2, C157.2, C18.2, C20.2, C24.2, C25.1, C26.1, C27.1, C29.2, C3.1, C30.2, C31.2, C33.2, C34.2, C35.2, C36.1, C37.2, C38.2, C39.1, C4.-, C41.2, C42.-, C43.2, C44.2, C5.-, C52.1, C53.2, C54.1, C55.1, C56.1, C57.1, C58.1, C59.2, C6.2, C60.1, C61.1, C64.2, C65.2, C66.-, C67.2, C68.1, C69.1, C7.2, C70.1, C71.2, C72.1, C73.1, C74.1, C75.1, C76.1, C77.1, C78.1, C8.2, C81.1, C82.1, D1.1, D1.2, D22.A, D23.A, D24.A, D25.A, D26.A, D28.1, D3.1, D3.2, D5.1, D5.2, D8.C, D9.A, GND.P$1, IC1.TP, IC10.4, IC11.8, IC13.3, IC14.3, IC14.4, IC14.5, IC14.8, IC2.5, IC21.1, IC22.2, IC22.8, IC23.8, IC24.8, IC25.1, IC26.2, IC26.8, IC27.7, IC28.4, IC29.29, IC3.2, IC3.3, IC3.6, IC3.7, IC32.4, IC33.3, IC33.4, IC34.3, IC35.4, IC4.12, IC4.9, IC5.4, IC7.5, IC9.4, IC9.5, IC9.9, JP3.2, K_PAR.A1, K_S1.8, K_S2.8, K_SER.A1, L1.4, LCD1.1, MCU.GND, MCU.GND1, MCU.GND2, MCU.GND3, MCU.GND4, MCU.ICSP_GND, OK3.3, Q15.2, Q16.E, Q18.E, Q27.2, Q29.2, Q30.2, Q8.2, R1.2, R126.1, R129.2, R131.1, R132.2, R133.2, R145.1, R149.2, R150.2, R17.1, R20.2, R22.2, R25.2, R26.2, R42.1, R44.1, R48.1, R60.1, R75.1, R8.1, R84.1, R91.1, R95.2, R96.1, RN1.5, RN1.6, RN1.7, RN1.8, RN2.5, SH1.P$2, SH2.P$2, SH3.P$1, SW2.1, SW2.2, SW2.5, TP2.GND, TR1.4, WIFI.1, X12.1, X12.1.1, X16.1, X16.2, X16.9, X19.4, X20.4, X3.10, X3.12, X3.14, ZD12.A
- net GND1: now also C158.1, C160.1, C162.2, C163.1, C164.1, C165.2, C166.1, C167.1, C168.1, C173.1, C174.2, C178.2, C179.2, C180.1, C181.1, C182.1, C183.1, C184.1, C185.1, C186.1, C187.1, C188.2, C189.2, C190.2, C191.2, C193.2, C194.2, C197.2, C204.2, C205.1, C206.2, C207.2, C208.1, C209.1, C212.1, C213.2, C214.2, C215.2, C216.2, C218.-, C219.2, C220.2, C221.2, C222.1, C223.-, C224.-, C225.-, C228.2, C233.1, C235.1, C236.1, C237.1, C238.1, C239.2, C240.2, D38.1, D38.2, D44.1, D44.2, D45.1, D45.2, D46.C, D47.A, GND1.P$1, IC36.8, IC37.3, IC37.4, IC37.5, IC37.8, IC38.4, IC38.5, IC38.9, IC41.5, IC42.4, IC43.TP, IC44.12, IC44.9, IC45.5, IC46.2, IC46.3, IC46.6, IC46.7, IC47.3, IC50.4, L17.4, Q40.2, Q42.2, Q48.E, Q49.E, R168.1, R184.1, R192.1, R197.1, R200.1, R214.1, R215.2, R219.1, R227.2, R228.2, R229.2, R232.2, R234.1, R238.2, R250.1, R253.1, SH4.P$2, SH5.P$2, TP6.GND, TR3.4, X21.10, X21.12, X21.14; no longer C10.2, C12.2, C18.2, C20.2, C24.2, C25.1, C26.1, C27.1, C29.2, C3.1, C30.2, C31.2, C33.2, C34.2, C35.2, C36.1, C37.2, C38.2, C39.1, C4.-, C41.2, C42.-, C43.2, C44.2, C5.-, C52.1, C53.2, C54.1, C55.1, C56.1, C57.1, C58.1, C59.2, C6.2, C60.1, C61.1, C64.2, C65.2, C66.-, C67.2, C68.1, C69.1, C7.2, C70.1, C71.2, C72.1, C73.1, C74.1, C75.1, C76.1, C77.1, C78.1, C8.2, C81.1, C82.1, D1.1, D1.2, D3.1, D3.2, D5.1, D5.2, D8.C, D9.A, GND.P$1, IC1.TP, IC10.4, IC11.8, IC13.3, IC14.3, IC14.4, IC14.5, IC14.8, IC2.5, IC3.2, IC3.3, IC3.6, IC3.7, IC4.12, IC4.9, IC5.4, IC7.5, IC9.4, IC9.5, IC9.9, L1.4, Q15.2, Q16.E, Q18.E, Q8.2, R1.2, R17.1, R20.2, R22.2, R25.2, R26.2, R42.1, R44.1, R48.1, R60.1, R75.1, R8.1, R84.1, R91.1, R95.2, R96.1, SH1.P$2, SH2.P$2, TP2.GND, TR1.4, X3.10, X3.12, X3.14
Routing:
- net +5V: track 120.8 -> 902.9 mm, vias 4 -> 29
- net +5V2: track 593.2 -> 0.00 mm, vias 18 -> 0
- net GND: track 87.2 -> 500.0 mm, vias 33 -> 280
- net GND8: track 241.5 -> 0.00 mm, vias 135 -> 0
- net +5V3: track 188.9 -> 0.00 mm, vias 7 -> 0
- net EARTH2: track 187.5 -> 0.00 mm, vias 1 -> 0
- net EARTH: track 55.8 -> 243.3 mm, vias 1 -> 2
- net GND7: track 171.2 -> 0.00 mm, vias 112 -> 0
- net WIFI_CE: track 54.2 -> 53.5 mm
- removed copper zone on layer 1, net GND7
- removed copper zone on layer 16, net GND7
- removed copper zone on layer 1, net GND8
- removed copper zone on layer 16, net GND8
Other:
- board text removed: "*"
- board text removed: "* Check instructions for R13 installation"
